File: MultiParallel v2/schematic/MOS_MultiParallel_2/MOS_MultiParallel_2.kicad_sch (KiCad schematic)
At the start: 56 parts, among them J10 ., J11 ., J12 Conn_01x01, J13 ., J14 ., J15 ., J16 ., J25 ., J26 .Conn_01x01, J27 .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

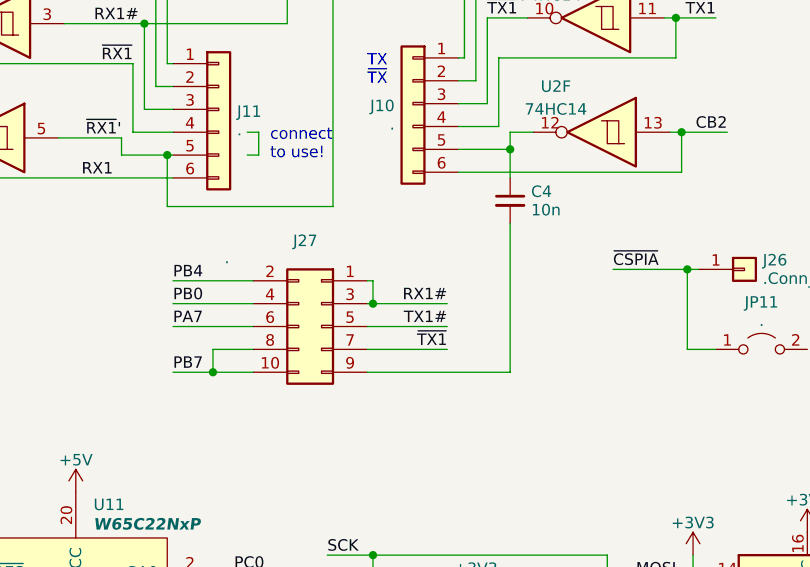
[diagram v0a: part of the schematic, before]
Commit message: SYM1 & KIM1 work, RAM Board update
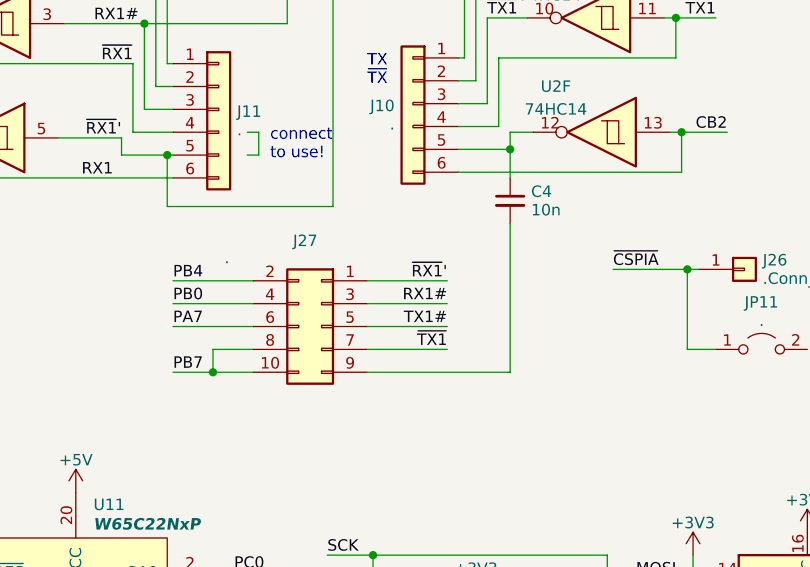
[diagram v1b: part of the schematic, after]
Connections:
- net RX1#: no longer J27.1 (Pin_1)
- net ~{RX1}': now also J27.1 (Pin_1)
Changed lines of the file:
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@@
     (company "100% Offner")
     (comment 1 "v1: Initial")
-    (comment 2 "v1.1: ~{DOE} is now ~{CS_ACIA} and ~{CS_ACIA2}")
+    (comment 2 "v1.1: ~{DOE} is now ~{CS_ACIA} and ~{CS_ACIA2}, J27-1 is now inverted.")
   )
   (junction (at 329.565 22.225) (diameter 0) (color 0 0 0 0)
@@
   )
   (junction (at 42.545 157.48) (diameter 0) (color 0 0 0 0)
-  )
-  (junction (at 295.91 66.04) (diameter 0) (color 0 0 0 0)
   )
   (junction (at 362.585 159.385) (diameter 0) (color 0 0 0 0)
@@
     (stroke (width 0) (type default))
   )
-  (wire (pts (xy 295.91 66.04) (xy 304.165 66.04))
+  (wire (pts (xy 295.275 66.04) (xy 304.165 66.04))
     (stroke (width 0) (type default))
   )
@@
     (stroke (width 0) (type default))
   )
+  (wire (pts (xy 295.275 63.5) (xy 304.165 63.5))
+    (stroke (width 0) (type default))
+  )
   (wire (pts (xy 273.685 41.91) (xy 271.78 41.91))
     (stroke (width 0) (type default))
@@
     (stroke (width 0) (type default))
   )
-  (wire (pts (xy 295.91 63.5) (xy 295.275 63.5))
-    (stroke (width 0) (type default))
-  )
   (wire (pts (xy 354.33 104.14) (xy 366.395 104.14))
     (stroke (width 0) (type default))
@@
     (stroke (width 0) (type default))
   )
-  (wire (pts (xy 295.275 66.04) (xy 295.91 66.04))
-    (stroke (width 0) (type default))
-  )
   (wire (pts (xy 229.87 26.67) (xy 238.125 26.67))
     (stroke (width 0) (type default))
@@
   )
   (wire (pts (xy 34.29 117.475) (xy 34.29 121.285))
-    (stroke (width 0) (type default))
-  )
-  (wire (pts (xy 295.91 66.04) (xy 295.91 63.5))
     (stroke (width 0) (type default))
   )
@@
     (effects (font (size 1.27 1.27)) (justify left bottom))
   )
+  (label "~{RX1}'" (at 304.165 63.5 180) (fields_autoplaced)
+    (effects (font (size 1.27 1.27)) (justify right bottom))
+  )
   (label "PB1" (at 357.505 47.625 0) (fields_autoplaced)
